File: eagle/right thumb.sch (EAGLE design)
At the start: 12 parts, among them J1 B7B-ZR_(LF)(SN)

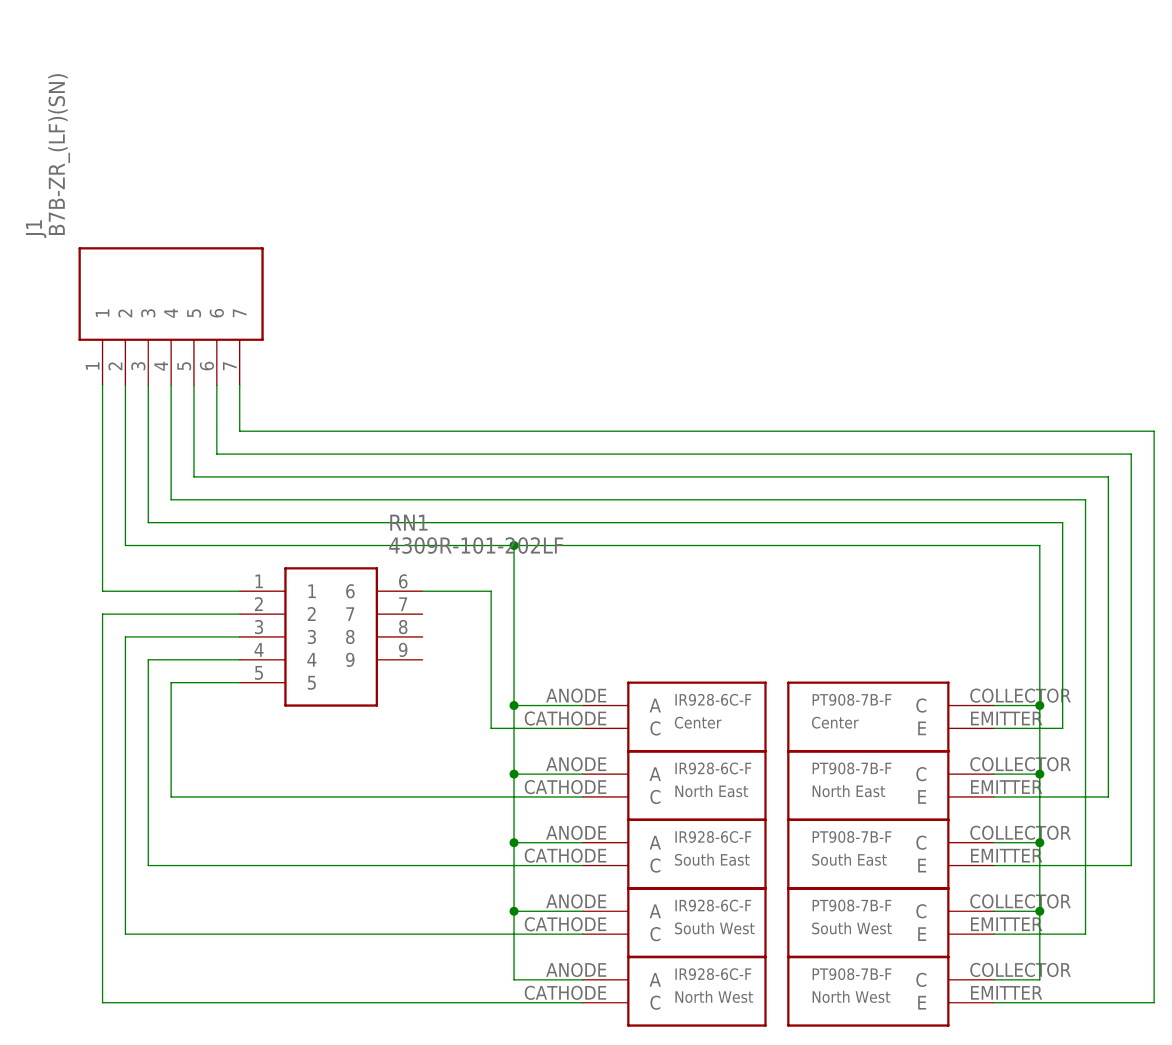
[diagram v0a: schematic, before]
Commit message: Reduce drill size of resistor holes. Fix right thumb cluster
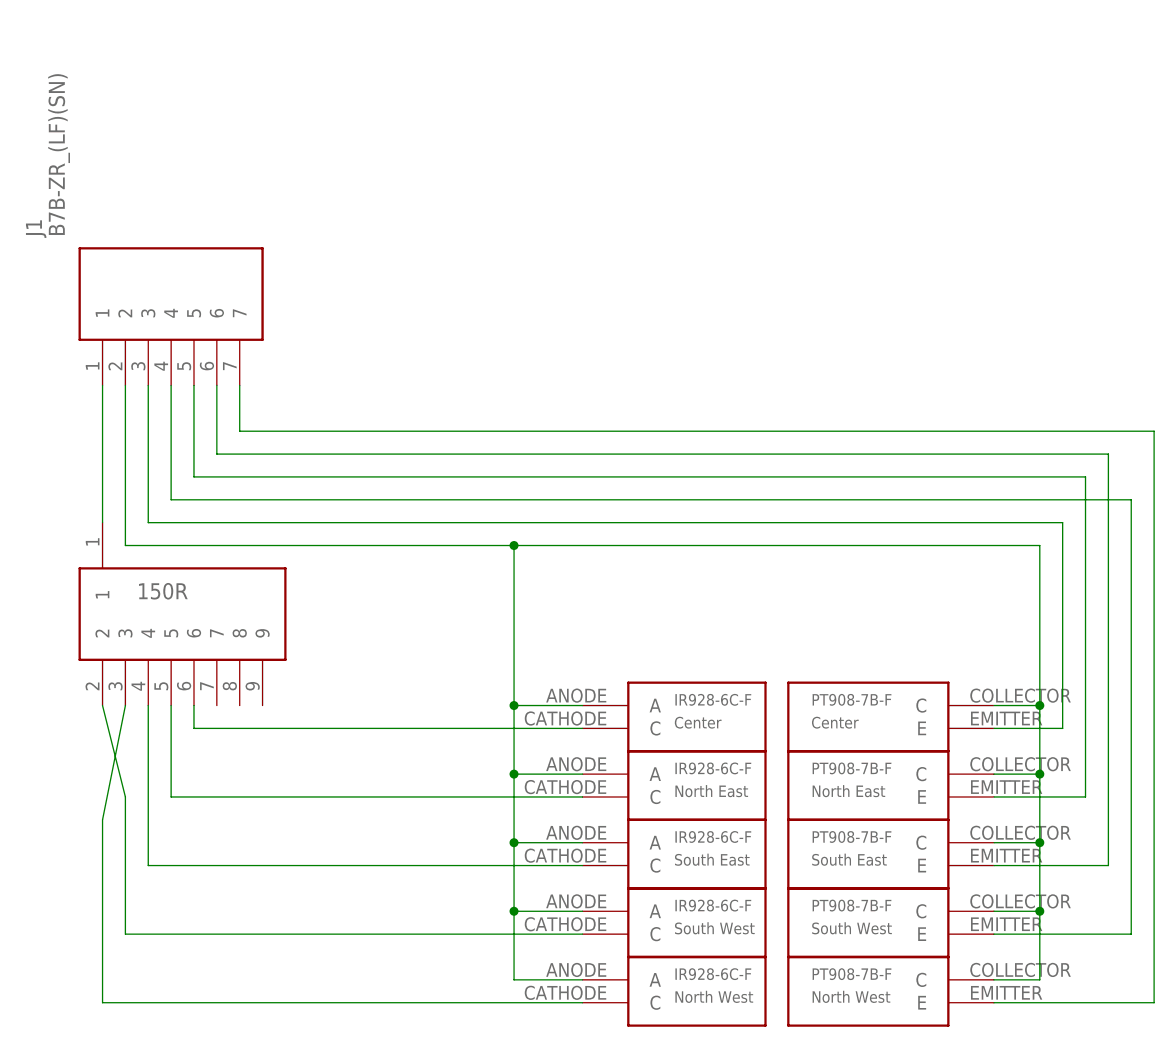
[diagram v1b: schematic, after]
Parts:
- RN1: value 4309R-101-202LF -> 150R; device 4309R-101-202LF:4309R-101-202LF -> 9 pin resistor network:9PIN-RESISTOR-NETWORK9PIN-RESISTOR-NETWORK
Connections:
- net N$2: now also RN1.3; no longer RN1.2
- net N$3: now also RN1.2; no longer RN1.3
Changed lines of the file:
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@@
 <?xml version="1.0" encoding="utf-8"?>
 <!DOCTYPE eagle SYSTEM "eagle.dtd">
-<eagle version="9.3.2">
+<eagle version="9.4.2">
 <drawing>
 <settings>
@@
 <part name="LED5" library="IR928-6C-F" deviceset="IR928-6C-F" device="" value="North West"/>
 <part name="J1" library="SamacSys_Parts" deviceset="B7B-ZR_(LF)(SN)" device=""/>
-<part name="RN1" library="4309R-101-202LF" deviceset="4309R-101-202LF" device=""/>
+<part name="RN1" library="9 pin resistor network" deviceset="9PIN-RESISTOR-NETWORK" device="9PIN-RESISTOR-NETWORK" value="150R"/>
 </parts>
 <sheets>
@@
 <attribute name="VALUE" x="7.62" y="90.17" size="1.778" layer="96" rot="R90" align="center-left"/>
 </instance>
-<instance part="RN1" gate="G$1" x="27.94" y="50.8" smashed="yes">
-<attribute name="NAME" x="44.45" y="58.42" size="1.778" layer="95" align="center-left"/>
-<attribute name="VALUE" x="44.45" y="55.88" size="1.778" layer="96" align="center-left"/>
+<instance part="RN1" gate="G$1" x="12.7" y="58.42" smashed="yes">
+<attribute name="VALUE" x="16.51" y="50.8" size="1.778" layer="96" align="center-left"/>
 </instance>
 </instances>
@@
 <pinref part="J1" gate="G$1" pin="1"/>
 <pinref part="RN1" gate="G$1" pin="1"/>
-<wire x1="12.7" y1="73.66" x2="12.7" y2="50.8" width="0.1524" layer="91"/>
-<wire x1="12.7" y1="50.8" x2="27.94" y2="50.8" width="0.1524" layer="91"/>
+<wire x1="12.7" y1="73.66" x2="12.7" y2="58.42" width="0.1524" layer="91"/>
 </segment>
 </net>
 <net name="N$2" class="0">
 <segment>
-<pinref part="RN1" gate="G$1" pin="2"/>
-<wire x1="27.94" y1="48.26" x2="12.7" y2="48.26" width="0.1524" layer="91"/>
 <pinref part="LED5" gate="G$1" pin="C"/>
-<wire x1="12.7" y1="48.26" x2="12.7" y2="5.08" width="0.1524" layer="91"/>
+<wire x1="12.7" y1="25.4" x2="12.7" y2="5.08" width="0.1524" layer="91"/>
 <wire x1="12.7" y1="5.08" x2="66.04" y2="5.08" width="0.1524" layer="91"/>
+<pinref part="RN1" gate="G$1" pin="3"/>
+<wire x1="15.24" y1="38.1" x2="12.7" y2="25.4" width="0.1524" layer="91"/>
 </segment>
 </net>
@@
 <pinref part="LED4" gate="G$1" pin="C"/>
 <wire x1="66.04" y1="12.7" x2="15.24" y2="12.7" width="0.1524" layer="91"/>
-<wire x1="15.24" y1="12.7" x2="15.24" y2="45.72" width="0.1524" layer="91"/>
-<pinref part="RN1" gate="G$1" pin="3"/>
-<wire x1="15.24" y1="45.72" x2="27.94" y2="45.72" width="0.1524" layer="91"/>
+<wire x1="15.24" y1="12.7" x2="15.24" y2="27.94" width="0.1524" layer="91"/>
+<pinref part="RN1" gate="G$1" pin="2"/>
+<wire x1="15.24" y1="27.94" x2="12.7" y2="38.1" width="0.1524" layer="91"/>
 </segment>
 </net>
@@
 <segment>
 <pinref part="RN1" gate="G$1" pin="4"/>
-<wire x1="27.94" y1="43.18" x2="17.78" y2="43.18" width="0.1524" layer="91"/>
-<wire x1="17.78" y1="43.18" x2="17.78" y2="20.32" width="0.1524" layer="91"/>
+<wire x1="17.78" y1="38.1" x2="17.78" y2="20.32" width="0.1524" layer="91"/>
 <pinref part="LED3" gate="G$1" pin="C"/>
 <wire x1="17.78" y1="20.32" x2="66.04" y2="20.32" width="0.1524" layer="91"/>
@@
 <wire x1="66.04" y1="27.94" x2="20.32" y2="27.94" width="0.1524" layer="91"/>
 <pinref part="RN1" gate="G$1" pin="5"/>
-<wire x1="20.32" y1="27.94" x2="20.32" y2="40.64" width="0.1524" layer="91"/>
-<wire x1="20.32" y1="40.64" x2="27.94" y2="40.64" width="0.1524" layer="91"/>
+<wire x1="20.32" y1="27.94" x2="20.32" y2="38.1" width="0.1524" layer="91"/>
 </segment>
 </net>
@@
 <segment>
 <pinref part="RN1" gate="G$1" pin="6"/>
-<wire x1="48.26" y1="50.8" x2="55.88" y2="50.8" width="0.1524" layer="91"/>
-<wire x1="55.88" y1="50.8" x2="55.88" y2="35.56" width="0.1524" layer="91"/>
+<wire x1="22.86" y1="38.1" x2="22.86" y2="35.56" width="0.1524" layer="91"/>
+<wire x1="22.86" y1="35.56" x2="66.04" y2="35.56" width="0.1524" layer="91"/>
 <pinref part="LED1" gate="G$1" pin="C"/>
-<wire x1="55.88" y1="35.56" x2="66.04" y2="35.56" width="0.1524" layer="91"/>
 </segment>
 </net>
@@
 <net name="N$8" class="0">
 <segment>
-<pinref part="PT1" gate="G$1" pin="E"/>
-<wire x1="111.76" y1="35.56" x2="119.38" y2="35.56" width="0.1524" layer="91"/>
-<wire x1="119.38" y1="35.56" x2="119.38" y2="58.42" width="0.1524" layer="91"/>
-<wire x1="119.38" y1="58.42" x2="17.78" y2="58.42" width="0.1524" layer="91"/>
-<pinref part="J1" gate="G$1" pin="3"/>
-<wire x1="17.78" y1="58.42" x2="17.78" y2="73.66" width="0.1524" layer="91"/>
+<pinref part="J1" gate="G$1" pin="4"/>
+<wire x1="20.32" y1="73.66" x2="20.32" y2="60.96" width="0.1524" layer="91"/>
+<wire x1="20.32" y1="60.96" x2="127" y2="60.96" width="0.1524" layer="91"/>
+<pinref part="PT4" gate="G$1" pin="E"/>
+<wire x1="127" y1="60.96" x2="127" y2="12.7" width="0.1524" layer="91"/>
+<wire x1="127" y1="12.7" x2="111.76" y2="12.7" width="0.1524" layer="91"/>
 </segment>
 </net>
 <net name="N$9" class="0">
 <segment>
-<pinref part="PT2" gate="G$1" pin="E"/>
-<wire x1="111.76" y1="27.94" x2="124.46" y2="27.94" width="0.1524" layer="91"/>
-<wire x1="124.46" y1="27.94" x2="124.46" y2="63.5" width="0.1524" layer="91"/>
-<wire x1="124.46" y1="63.5" x2="22.86" y2="63.5" width="0.1524" layer="91"/>
+<pinref part="J1" gate="G$1" pin="6"/>
+<wire x1="25.4" y1="66.04" x2="25.4" y2="73.66" width="0.1524" layer="91"/>
+<wire x1="25.4" y1="66.04" x2="124.46" y2="66.04" width="0.1524" layer="91"/>
+<pinref part="PT3" gate="G$1" pin="E"/>
+<wire x1="124.46" y1="66.04" x2="124.46" y2="20.32" width="0.1524" layer="91"/>
+<wire x1="124.46" y1="20.32" x2="111.76" y2="20.32" width="0.1524" layer="91"/>
+</segment>
+</net>
+<net name="N$10" class="0">
+<segment>
 <pinref part="J1" gate="G$1" pin="5"/>
 <wire x1="22.86" y1="63.5" x2="22.86" y2="73.66" width="0.1524" layer="91"/>
-</segment>
-</net>
-<net name="N$10" class="0">
-<segment>
-<pinref part="PT3" gate="G$1" pin="E"/>
-<wire x1="111.76" y1="20.32" x2="127" y2="20.32" width="0.1524" layer="91"/>
-<wire x1="127" y1="20.32" x2="127" y2="66.04" width="0.1524" layer="91"/>
-<pinref part="J1" gate="G$1" pin="6"/>
-<wire x1="127" y1="66.04" x2="25.4" y2="66.04" width="0.1524" layer="91"/>
-<wire x1="25.4" y1="66.04" x2="25.4" y2="73.66" width="0.1524" layer="91"/>
+<wire x1="22.86" y1="63.5" x2="121.92" y2="63.5" width="0.1524" layer="91"/>
+<pinref part="PT2" gate="G$1" pin="E"/>
+<wire x1="121.92" y1="63.5" x2="121.92" y2="27.94" width="0.1524" layer="91"/>
+<wire x1="121.92" y1="27.94" x2="111.76" y2="27.94" width="0.1524" layer="91"/>
 </segment>
 </net>
 <net name="N$11" class="0">
 <segment>
-<pinref part="PT4" gate="G$1" pin="E"/>
-<wire x1="111.76" y1="12.7" x2="121.92" y2="12.7" width="0.1524" layer="91"/>
-<wire x1="121.92" y1="12.7" x2="121.92" y2="60.96" width="0.1524" layer="91"/>
-<pinref part="J1" gate="G$1" pin="4"/>
-<wire x1="121.92" y1="60.96" x2="20.32" y2="60.96" width="0.1524" layer="91"/>
-<wire x1="20.32" y1="60.96" x2="20.32" y2="73.66" width="0.1524" layer="91"/>
-</segment>
-</net>
-<net name="N$12" class="0">
-<segment>
-<pinref part="PT5" gate="G$1" pin="E"/>
-<wire x1="111.76" y1="5.08" x2="129.54" y2="5.08" width="0.1524" layer="91"/>
-<wire x1="129.54" y1="5.08" x2="129.54" y2="68.58" width="0.1524" layer="91"/>
-<wire x1="129.54" y1="68.58" x2="27.94" y2="68.58" width="0.1524" layer="91"/>
 <pinref part="J1" gate="G$1" pin="7"/>
 <wire x1="27.94" y1="68.58" x2="27.94" y2="73.66" width="0.1524" layer="91"/>
-</segment>
-</net>
+<wire x1="27.94" y1="68.58" x2="129.54" y2="68.58" width="0.1524" layer="91"/>
+<pinref part="PT5" gate="G$1" pin="E"/>
+<wire x1="129.54" y1="68.58" x2="129.54" y2="5.08" width="0.1524" layer="91"/>
+<wire x1="129.54" y1="5.08" x2="111.76" y2="5.08" width="0.1524" layer="91"/>
+</segment>
+</net>
+<net name="N$12" class="0">
+<segment>
+<pinref part="J1" gate="G$1" pin="3"/>
+<wire x1="17.78" y1="73.66" x2="17.78" y2="58.42" width="0.1524" layer="91"/>
+<wire x1="17.78" y1="58.42" x2="119.38" y2="58.42" width="0.1524" layer="91"/>
+<pinref part="PT1" gate="G$1" pin="E"/>
+<wire x1="119.38" y1="58.42" x2="119.38" y2="35.56" width="0.1524" layer="91"/>
+<wire x1="119.38" y1="35.56" x2="111.76" y2="35.56" width="0.1524" layer="91"/>
+</segment>
+</net>
